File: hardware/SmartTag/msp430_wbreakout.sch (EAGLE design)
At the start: 16 parts, among them U1 ADXL362

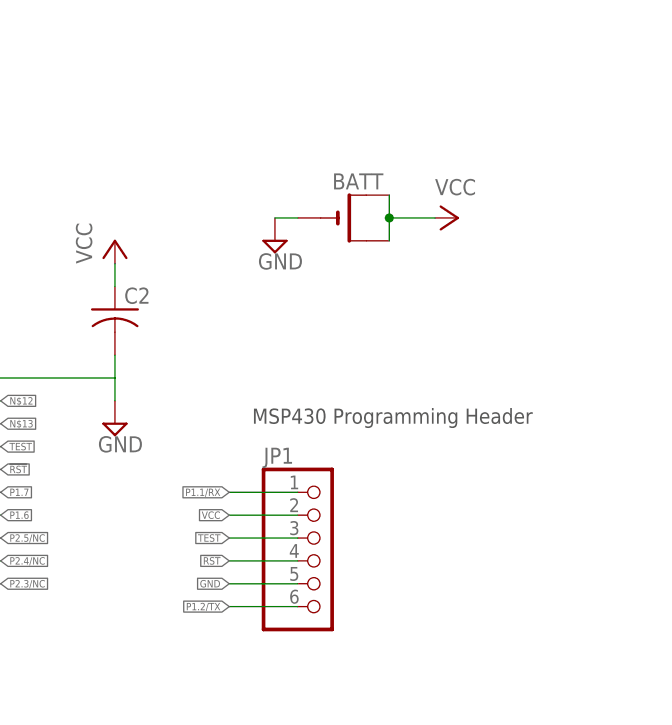
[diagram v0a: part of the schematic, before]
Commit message: hw: Add status LED and capacitive sensor headers
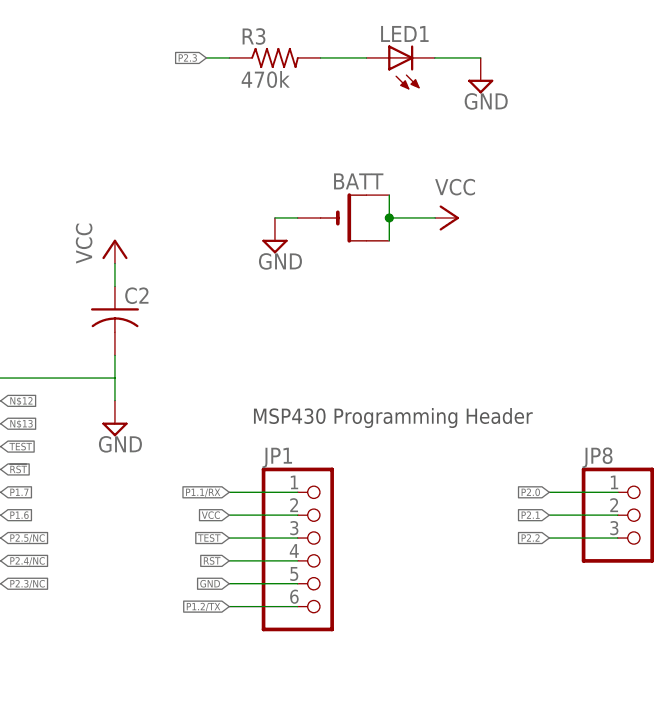
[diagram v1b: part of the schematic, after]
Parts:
- added JP8: (no value), pinhead:PINHD-1X3
- added LED1: (no value), led:LEDCHIP-LED0805
- added R3: 470k, rcl:R-US_R0805
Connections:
- new net N$1: LED1.A, R3.2
- new net P2.3: R3.1
- net GND: now also LED1.C
- net P2.0: now also JP8.1
- net P2.1: now also JP8.2
- net P2.2: now also JP8.3
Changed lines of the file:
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@@
 <grid distance="0.1" unitdist="inch" unit="inch" style="lines" multiple="1" display="yes" altdistance="0.01" altunitdist="inch" altunit="inch"/>
 <layers>
-<layer number="1" name="Top" color="4" fill="1" visible="yes" active="no"/>
-<layer number="16" name="Bottom" color="1" fill="1" visible="yes" active="no"/>
-<layer number="17" name="Pads" color="2" fill="1" visible="yes" active="no"/>
-<layer number="18" name="Vias" color="2" fill="1" visible="yes" active="no"/>
-<layer number="19" name="Unrouted" color="6" fill="1" visible="yes" active="no"/>
-<layer number="20" name="Dimension" color="15" fill="1" visible="yes" active="no"/>
-<layer number="21" name="tPlace" color="7" fill="1" visible="yes" active="no"/>
-<layer number="22" name="bPlace" color="7" fill="1" visible="yes" active="no"/>
-<layer number="23" name="tOrigins" color="15" fill="1" visible="yes" active="no"/>
-<layer number="24" name="bOrigins" color="15" fill="1" visible="yes" active="no"/>
-<layer number="25" name="tNames" color="7" fill="1" visible="yes" active="no"/>
-<layer number="26" name="bNames" color="7" fill="1" visible="yes" active="no"/>
-<layer number="27" name="tValues" color="7" fill="1" visible="yes" active="no"/>
-<layer number="28" name="bValues" color="7" fill="1" visible="yes" active="no"/>
+<layer number="1" name="Top" color="4" fill="1" visible="no" active="no"/>
+<layer number="16" name="Bottom" color="1" fill="1" visible="no" active="no"/>
+<layer number="17" name="Pads" color="2" fill="1" visible="no" active="no"/>
+<layer number="18" name="Vias" color="2" fill="1" visible="no" active="no"/>
+<layer number="19" name="Unrouted" color="6" fill="1" visible="no" active="no"/>
+<layer number="20" name="Dimension" color="15" fill="1" visible="no" active="no"/>
+<layer number="21" name="tPlace" color="7" fill="1" visible="no" active="no"/>
+<layer number="22" name="bPlace" color="7" fill="1" visible="no" active="no"/>
+<layer number="23" name="tOrigins" color="15" fill="1" visible="no" active="no"/>
+<layer number="24" name="bOrigins" color="15" fill="1" visible="no" active="no"/>
+<layer number="25" name="tNames" color="7" fill="1" visible="no" active="no"/>
+<layer number="26" name="bNames" color="7" fill="1" visible="no" active="no"/>
+<layer number="27" name="tValues" color="7" fill="1" visible="no" active="no"/>
+<layer number="28" name="bValues" color="7" fill="1" visible="no" active="no"/>
 <layer number="29" name="tStop" color="7" fill="3" visible="no" active="no"/>
 <layer number="30" name="bStop" color="7" fill="6" visible="no" active="no"/>
@@
 <layer number="35" name="tGlue" color="7" fill="4" visible="no" active="no"/>
 <layer number="36" name="bGlue" color="7" fill="5" visible="no" active="no"/>
-<layer number="37" name="tTest" color="7" fill="1" visible="yes" active="no"/>
-<layer number="38" name="bTest" color="7" fill="1" visible="yes" active="no"/>
+<layer number="37" name="tTest" color="7" fill="1" visible="no" active="no"/>
+<layer number="38" name="bTest" color="7" fill="1" visible="no" active="no"/>
 <layer number="39" name="tKeepout" color="4" fill="11" visible="no" active="no"/>
 <layer number="40" name="bKeepout" color="1" fill="11" visible="no" active="no"/>
@@
 <layer number="44" name="Drills" color="7" fill="1" visible="no" active="no"/>
 <layer number="45" name="Holes" color="7" fill="1" visible="no" active="no"/>
-<layer number="46" name="Milling" color="3" fill="1" visible="yes" active="no"/>
-<layer number="47" name="Measures" color="7" fill="1" visible="yes" active="no"/>
-<layer number="48" name="Document" color="7" fill="1" visible="yes" active="no"/>
-<layer number="49" name="Reference" color="7" fill="1" visible="yes" active="no"/>
-<layer number="50" name="dxf" color="7" fill="1" visible="yes" active="no"/>
-<layer number="51" name="tDocu" color="7" fill="1" visible="yes" active="no"/>
-<layer number="52" name="bDocu" color="7" fill="1" visible="yes" active="no"/>
-<layer number="53" name="tGND_GNDA" color="7" fill="9" visible="yes" active="no"/>
-<layer number="54" name="bGND_GNDA" color="1" fill="9" visible="yes" active="no"/>
-<layer number="56" name="wert" color="7" fill="1" visible="yes" active="no"/>
-<layer number="57" name="tCAD" color="7" fill="1" visible="yes" active="no"/>
-<layer number="59" name="tCarbon" color="7" fill="1" visible="yes" active="no"/>
-<layer number="60" name="bCarbon" color="7" fill="1" visible="yes" active="no"/>
+<layer number="46" name="Milling" color="3" fill="1" visible="no" active="no"/>
+<layer number="47" name="Measures" color="7" fill="1" visible="no" active="no"/>
+<layer number="48" name="Document" color="7" fill="1" visible="no" active="no"/>
+<layer number="49" name="Reference" color="7" fill="1" visible="no" active="no"/>
+<layer number="50" name="dxf" color="7" fill="1" visible="no" active="no"/>
+<layer number="51" name="tDocu" color="7" fill="1" visible="no" active="no"/>
+<layer number="52" name="bDocu" color="7" fill="1" visible="no" active="no"/>
+<layer number="53" name="tGND_GNDA" color="7" fill="9" visible="no" active="no"/>
+<layer number="54" name="bGND_GNDA" color="1" fill="9" visible="no" active="no"/>
+<layer number="56" name="wert" color="7" fill="1" visible="no" active="no"/>
+<layer number="57" name="tCAD" color="7" fill="1" visible="no" active="no"/>
+<layer number="59" name="tCarbon" color="7" fill="1" visible="no" active="no"/>
+<layer number="60" name="bCarbon" color="7" fill="1" visible="no" active="no"/>
 <layer number="90" name="Modules" color="5" fill="1" visible="yes" active="yes"/>
 <layer number="91" name="Nets" color="2" fill="1" visible="yes" active="yes"/>
@@
 <part name="JP6" library="pinhead" deviceset="PINHD-1X4" device=""/>
 <part name="JP7" library="pinhead" deviceset="PINHD-1X4" device=""/>
+<part name="LED1" library="led" deviceset="LED" device="CHIP-LED0805"/>
+<part name="R3" library="rcl" deviceset="R-US_" device="R0805" value="470k"/>
+<part name="SUPPLY5" library="supply2" deviceset="GND" device=""/>
+<part name="JP8" library="pinhead" deviceset="PINHD-1X3" device=""/>
 </parts>
 <sheets>
@@
 <instance part="JP6" gate="A" x="116.84" y="20.32" rot="MR0"/>
 <instance part="JP7" gate="A" x="152.4" y="20.32"/>
+<instance part="LED1" gate="G$1" x="132.08" y="180.34" rot="R90"/>
+<instance part="R3" gate="G$1" x="119.38" y="180.34"/>
+<instance part="SUPPLY5" gate="GND" x="142.24" y="177.8"/>
+<instance part="JP8" gate="A" x="160.02" y="129.54"/>
 </instances>
 <busses>
@@
 <label x="30.48" y="127" size="0.8128" layer="91" ratio="31" rot="MR0" xref="yes"/>
 </segment>
+<segment>
+<pinref part="JP8" gate="A" pin="1"/>
+<wire x1="157.48" y1="132.08" x2="149.86" y2="132.08" width="0.1524" layer="91"/>
+<label x="149.86" y="132.08" size="0.8128" layer="91" rot="MR0" xref="yes"/>
+</segment>
 </net>
 <net name="P2.1" class="0">
@@
 <label x="30.48" y="124.46" size="0.8128" layer="91" ratio="31" rot="MR0" xref="yes"/>
 </segment>
+<segment>
+<pinref part="JP8" gate="A" pin="2"/>
+<wire x1="157.48" y1="129.54" x2="149.86" y2="129.54" width="0.1524" layer="91"/>
+<label x="149.86" y="129.54" size="0.8128" layer="91" rot="MR0" xref="yes"/>
+</segment>
 </net>
 <net name="P2.2" class="0">
@@
 <wire x1="36.83" y1="121.92" x2="30.48" y2="121.92" width="0.1524" layer="91"/>
 <label x="30.48" y="121.92" size="0.8128" layer="91" ratio="31" rot="MR0" xref="yes"/>
+</segment>
+<segment>
+<pinref part="JP8" gate="A" pin="3"/>
+<wire x1="157.48" y1="127" x2="149.86" y2="127" width="0.1524" layer="91"/>
+<label x="149.86" y="127" size="0.8128" layer="91" rot="MR0" xref="yes"/>
 </segment>
 </net>
@@
 <label x="142.24" y="25.4" size="0.8128" layer="91" rot="MR0" xref="yes"/>
 </segment>
+<segment>
+<pinref part="LED1" gate="G$1" pin="C"/>
+<pinref part="SUPPLY5" gate="GND" pin="GND"/>
+<wire x1="137.16" y1="180.34" x2="142.24" y2="180.34" width="0.1524" layer="91"/>
+</segment>
 </net>
 <net name="RF1P" class="0">
@@
 </segment>
 </net>
+<net name="N$1" class="0">
+<segment>
+<pinref part="R3" gate="G$1" pin="2"/>
+<pinref part="LED1" gate="G$1" pin="A"/>
+<wire x1="124.46" y1="180.34" x2="129.54" y2="180.34" width="0.1524" layer="91"/>
+</segment>
+</net>
+<net name="P2.3" class="0">
+<segment>
+<pinref part="R3" gate="G$1" pin="1"/>
+<wire x1="114.3" y1="180.34" x2="111.76" y2="180.34" width="0.1524" layer="91"/>
+<label x="111.76" y="180.34" size="0.8128" layer="91" rot="MR0" xref="yes"/>
+</segment>
+</net>

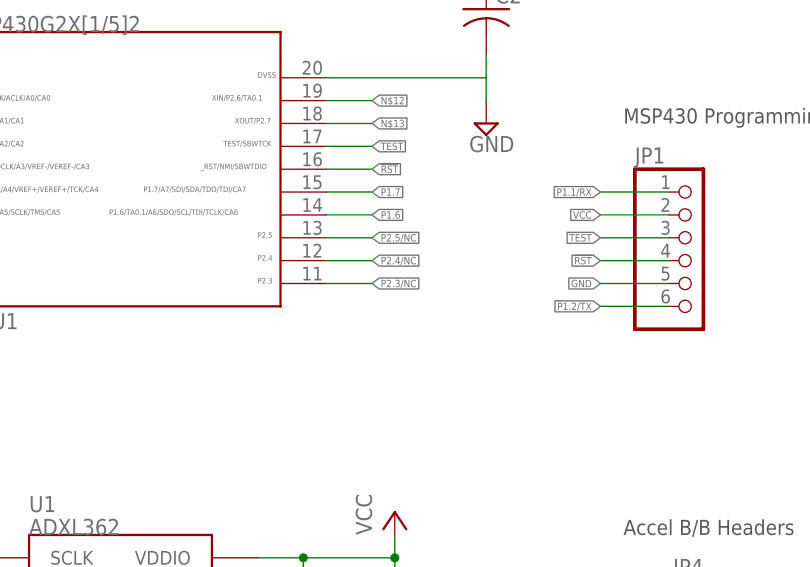
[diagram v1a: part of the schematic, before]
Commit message: hw: Add LED to schematic and board.
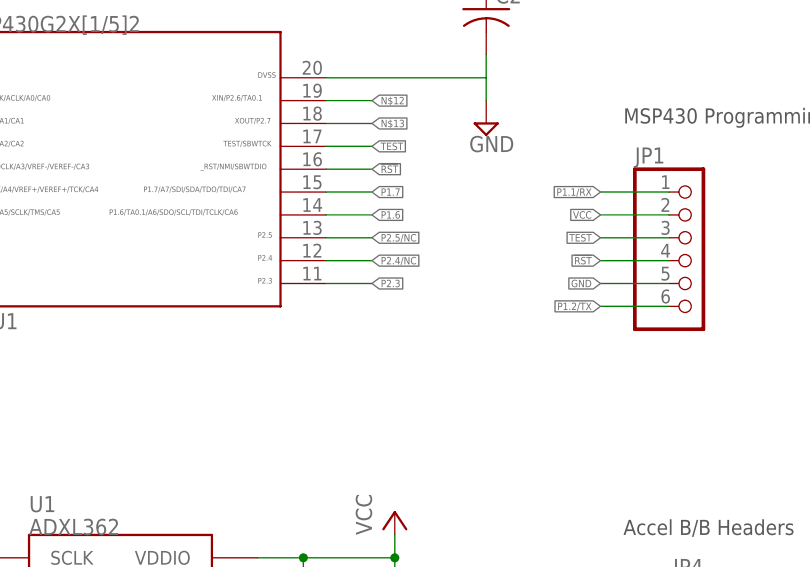
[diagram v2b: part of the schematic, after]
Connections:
- removed net P2.3/NC: MCU1.11
- net P2.3: now also MCU1.11
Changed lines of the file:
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@@
 <setting verticaltext="up"/>
 </settings>
-<grid distance="0.1" unitdist="inch" unit="inch" style="lines" multiple="1" display="yes" altdistance="0.01" altunitdist="inch" altunit="inch"/>
+<grid distance="0.1" unitdist="inch" unit="inch" style="lines" multiple="1" display="no" altdistance="0.01" altunitdist="inch" altunit="inch"/>
 <layers>
 <layer number="1" name="Top" color="4" fill="1" visible="no" active="no"/>
@@
 </segment>
 </net>
-<net name="P2.3/NC" class="0">
-<segment>
-<pinref part="MCU1" gate="G$1" pin="11"/>
-<wire x1="83.82" y1="121.92" x2="88.9" y2="121.92" width="0.1524" layer="91"/>
-<label x="88.9" y="121.92" size="0.8128" layer="91" ratio="31" xref="yes"/>
-</segment>
-</net>
 <net name="GND" class="0">
 <segment>
@@
 <label x="111.76" y="180.34" size="0.8128" layer="91" rot="MR0" xref="yes"/>
 </segment>
-</net>
+<segment>
+<pinref part="MCU1" gate="G$1" pin="11"/>
+<wire x1="83.82" y1="121.92" x2="88.9" y2="121.92" width="0.1524" layer="91"/>
+<label x="88.9" y="121.92" size="0.8128" layer="91" ratio="31" xref="yes"/>
+</segment>
+</net>
